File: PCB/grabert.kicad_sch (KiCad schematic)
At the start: 72 parts, among them J1 Conn_01x02, J2 Conn_01x02, J3 Conn_01x05, J4 USB_C_Receptacle_USB2.0, J5 SSD1306, SW0_0 1.00u, SW0_1 1.00u, SW0_10 1.00u, SW0_11 1.00u, SW0_12 1.00u, SW0_13-14 2.00u_or_1.00and1.00, SW0_2 1.00u, SW0_3 1.00u, SW0_4 1.00u, SW0_5 1.00u, SW0_6 1.00u, SW0_7 1.00u, SW0_8 1.00u, SW0_9 1.00u, SW1 RotaryEncoder_Switch, SW1_0 1.50u, SW1_1 1.00u, SW1_10 1.00u, SW1_11 1.00u, SW1_12 1.00u, SW1_13 1.50u, SW1_2 1.00u, SW1_3 1.00u, SW1_4 1.00u, SW1_5 1.00u, SW1_6 1.00u, SW1_7 1.00u, SW1_8 1.00u, SW1_9 1.00u, SW2_0 1.75u_stepped_caps_lock, SW2_1 1.00u, SW2_10 1.00u, SW2_11 1.00u, SW2_12 2.25u, SW2_2 1.00u, SW2_3 1.00u, SW2_4 1.00u, SW2_5 1.00u, SW2_6 1.00u, SW2_7 1.00u, SW2_8 1.00u, SW2_9 1.00u, SW3_0-1 2.25u_or_1.25and1.00, SW3_10 1.00u, SW3_11 1.00u, SW3_12-13 2.75u_or_1.75and1.00, SW3_2 1.00u, SW3_3 1.00u, SW3_4 1.00u, SW3_5 1.00u, SW3_6 1.00u, SW3_7 1.00u, SW3_8 1.00u, SW3_9 1.00u, SW4_0 1.25u, SW4_1 1.25u, SW4_2 1.25u, SW4_3 6.25u, SW4_4-8 4x1.25u_or_5x1.00u, U1 AMS1117-3.3, U2 STM32F072V8Tx

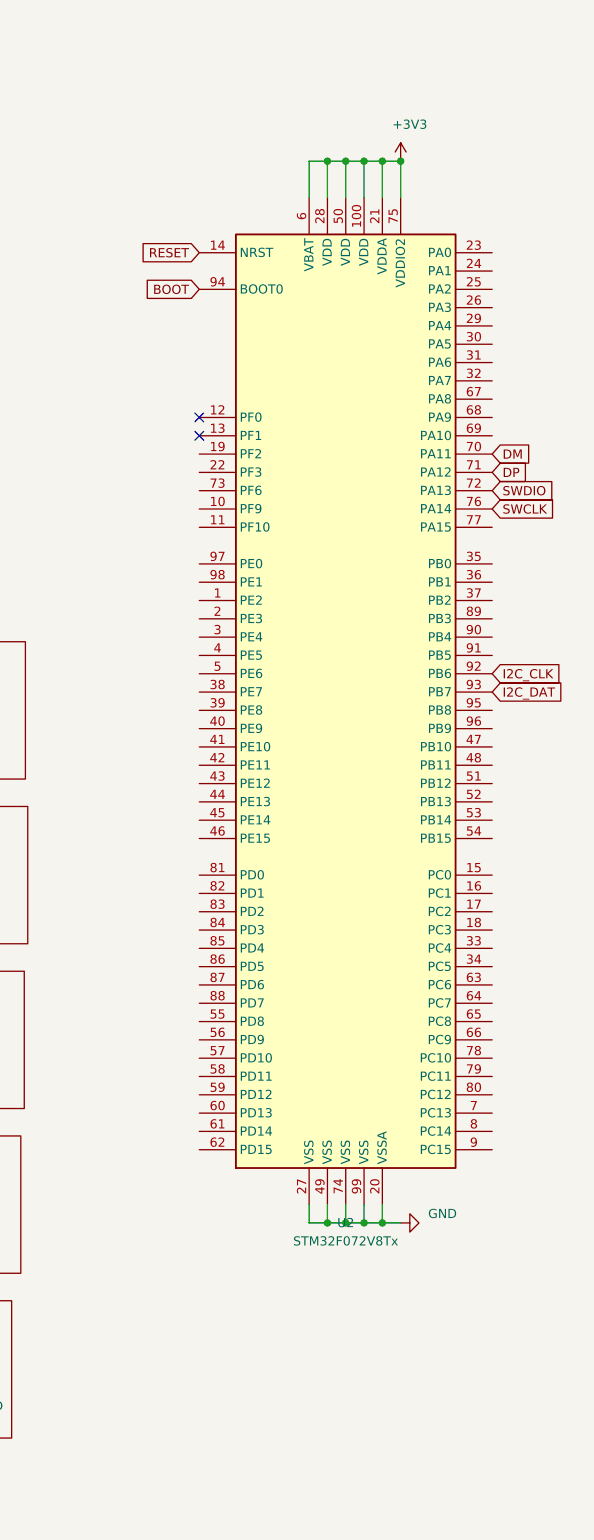
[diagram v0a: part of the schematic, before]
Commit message: Switch inputs linked to mcu
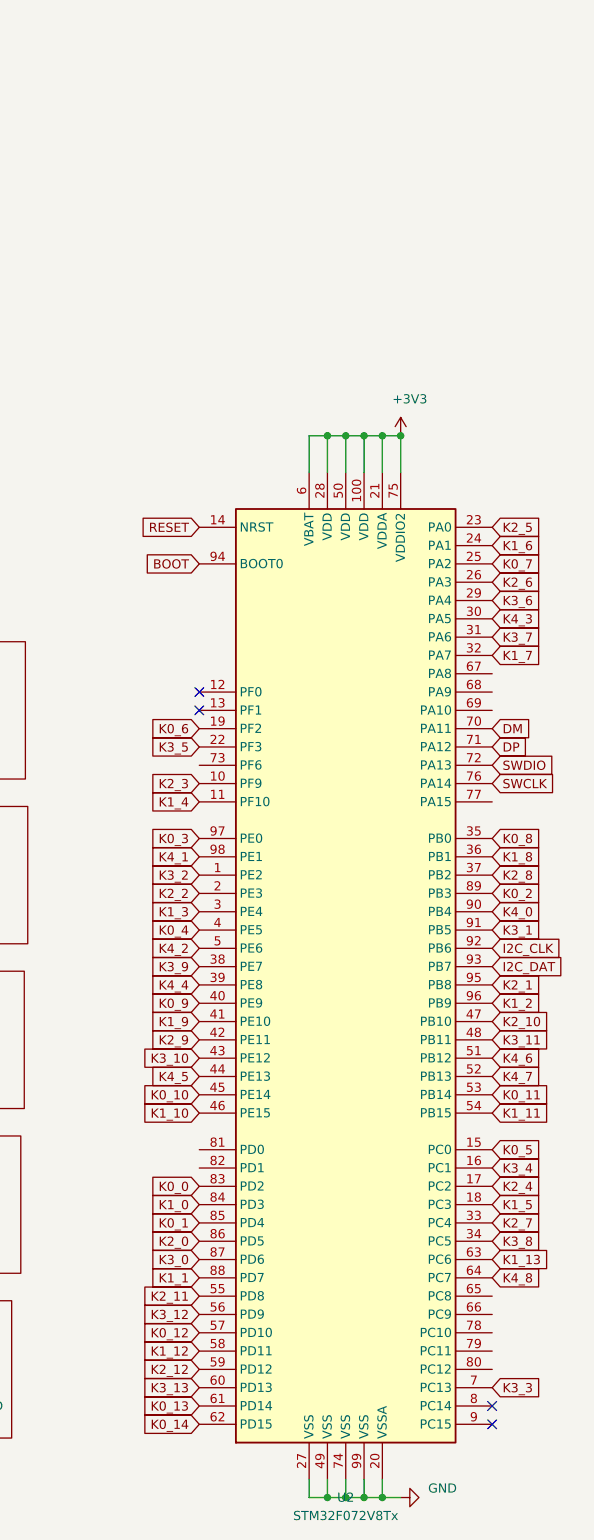
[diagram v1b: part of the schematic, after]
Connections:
- net K0_0: now also U2.83 (PD2)
- net K0_1: now also U2.85 (PD4)
- net K0_10: now also U2.45 (PE14)
- net K0_11: now also U2.53 (PB14)
- net K0_12: now also U2.57 (PD10)
- net K0_13: now also U2.61 (PD14)
- net K0_14: now also U2.62 (PD15)
- net K0_2: now also U2.89 (PB3)
- net K0_3: now also U2.97 (PE0)
- net K0_4: now also U2.4 (PE5)
- net K0_5: now also U2.15 (PC0)
- net K0_6: now also U2.19 (PF2)
- net K0_7: now also U2.25 (PA2)
- net K0_8: now also U2.35 (PB0)
- net K0_9: now also U2.40 (PE9)
- net K1_0: now also U2.84 (PD3)
- net K1_1: now also U2.88 (PD7)
- net K1_10: now also U2.46 (PE15)
- net K1_11: now also U2.54 (PB15)
- net K1_12: now also U2.58 (PD11)
- net K1_13: now also U2.63 (PC6)
- net K1_2: now also U2.96 (PB9)
- net K1_3: now also U2.3 (PE4)
- net K1_4: now also U2.11 (PF10)
- net K1_5: now also U2.18 (PC3)
- net K1_6: now also U2.24 (PA1)
- net K1_7: now also U2.32 (PA7)
- net K1_8: now also U2.36 (PB1)
- net K1_9: now also U2.41 (PE10)
- net K2_0: now also U2.86 (PD5)
- net K2_1: now also U2.95 (PB8)
- net K2_10: now also U2.47 (PB10)
- net K2_11: now also U2.55 (PD8)
- net K2_12: now also U2.59 (PD12)
- net K2_2: now also U2.2 (PE3)
- net K2_3: now also U2.10 (PF9)
- net K2_4: now also U2.17 (PC2)
- net K2_5: now also U2.23 (PA0)
- net K2_6: now also U2.26 (PA3)
- net K2_7: now also U2.33 (PC4)
- net K2_8: now also U2.37 (PB2)
- net K2_9: now also U2.42 (PE11)
- net K3_0: now also U2.87 (PD6)
- net K3_1: now also U2.91 (PB5)
- net K3_10: now also U2.43 (PE12)
- net K3_11: now also U2.48 (PB11)
- net K3_12: now also U2.56 (PD9)
- net K3_13: now also U2.60 (PD13)
- net K3_2: now also U2.1 (PE2)
- net K3_3: now also U2.7 (PC13)
- net K3_4: now also U2.16 (PC1)
- net K3_5: now also U2.22 (PF3)
- net K3_6: now also U2.29 (PA4)
- net K3_7: now also U2.31 (PA6)
- net K3_8: now also U2.34 (PC5)
- net K3_9: now also U2.38 (PE7)
- net K4_0: now also U2.90 (PB4)
- net K4_1: now also U2.98 (PE1)
- net K4_2: now also U2.5 (PE6)
- net K4_3: now also U2.30 (PA5)
- net K4_4: now also U2.39 (PE8)
- net K4_5: now also U2.44 (PE13)
- net K4_6: now also U2.51 (PB12)
- net K4_7: now also U2.52 (PB13)
- net K4_8: now also U2.64 (PC7)
- no-connect marks 6 -> 8
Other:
- moved on the sheet: U2

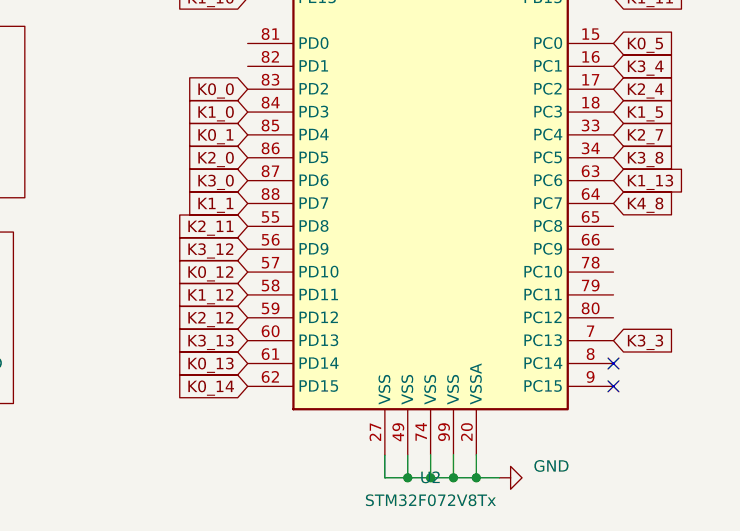
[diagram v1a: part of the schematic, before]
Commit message: right switch traces
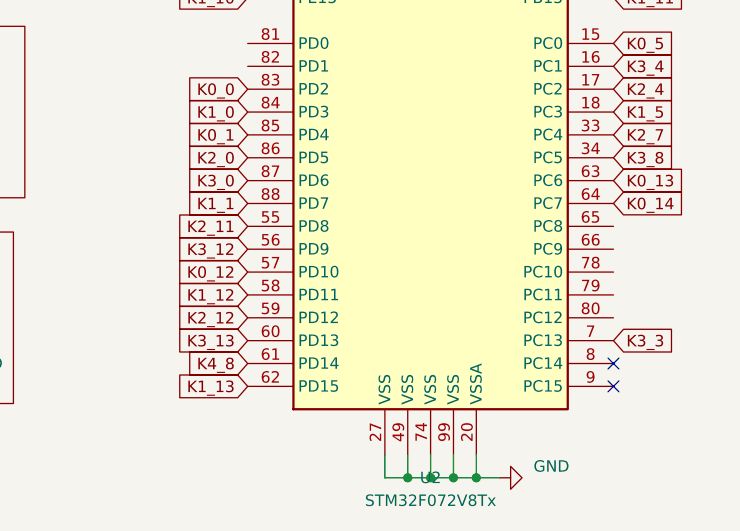
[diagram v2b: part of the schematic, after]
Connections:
- net K0_13: now also U2.63 (PC6); no longer U2.61 (PD14)
- net K0_14: now also U2.64 (PC7); no longer U2.62 (PD15)
- net K1_13: now also U2.62 (PD15); no longer U2.63 (PC6)
- net K4_8: now also U2.61 (PD14); no longer U2.64 (PC7)
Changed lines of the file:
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@@
   (junction (at 378.46 226.06) (diameter 1.016) (color 0 0 0 0))
   (junction (at 381 78.74) (diameter 1.016) (color 0 0 0 0))
+  (no_connect (at 314.96 40.64))
+  (no_connect (at 393.7 213.36))
+  (no_connect (at 353.06 116.84))
+  (no_connect (at 314.96 36.83))
   (no_connect (at 228.6 62.23))
+  (no_connect (at 393.7 215.9))
+  (no_connect (at 228.6 64.77))
   (no_connect (at 353.06 114.3))
-  (no_connect (at 314.96 40.64))
-  (no_connect (at 314.96 36.83))
-  (no_connect (at 228.6 64.77))
-  (no_connect (at 353.06 116.84))
-  (no_connect (at 393.7 213.36))
-  (no_connect (at 393.7 215.9))
   (wire (pts (xy 38.1 38.1) (xy 45.72 38.1))
     (stroke (width 0) (type solid) (color 0 0 0 0))
@@
     (effects (font (size 1.27 1.27)) (justify right))
   )
-  (global_label "K0_13" (shape input) (at 353.06 213.36 180)
-    (effects (font (size 1.27 1.27)) (justify right))
-  )
-  (global_label "K0_14" (shape input) (at 353.06 215.9 180)
+  (global_label "K4_8" (shape input) (at 353.06 213.36 180)
+    (effects (font (size 1.27 1.27)) (justify right))
+  )
+  (global_label "K1_13" (shape input) (at 353.06 215.9 180)
     (effects (font (size 1.27 1.27)) (justify right))
   )
@@
     (effects (font (size 1.27 1.27)) (justify left))
   )
-  (global_label "K1_13" (shape input) (at 393.7 193.04 0)
-    (effects (font (size 1.27 1.27)) (justify left))
-  )
-  (global_label "K4_8" (shape input) (at 393.7 195.58 0)
-    (effects (font (size 1.27 1.27)) (justify left))
-  )
+  (global_label "K0_13" (shape input) (at 393.7 193.04 0)
+    (effects (font (size 1.27 1.27)) (justify left))
+  )
+  (global_label "K0_14" (shape input) (at 393.7 195.58 0)
+    (effects (font (size 1.27 1.27)) (justify left))
+  )

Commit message: Routed PCB
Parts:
- added J6: Conn_01x03, Connector_PinHeader_2.54mm:PinHeader_1x03_P2.54mm_Vertical, symbol Connector_Generic:Conn_01x03
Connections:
- net +5V: now also J6.3 (Pin_3)
- net ENC_A: now also U2.66 (PC9)
- net ENC_B: now also U2.67 (PA8)
- net ENC_SW: now also U2.65 (PC8)
- net GND: now also J6.2 (Pin_2)
- net PA9: now reaches U2.68 (PA9)
- net PA9: now also J6.1 (Pin_1)
- net DM renamed D_N
- net DP renamed D_P
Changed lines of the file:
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@@
   (junction (at 378.46 226.06) (diameter 1.016) (color 0 0 0 0))
   (junction (at 381 78.74) (diameter 1.016) (color 0 0 0 0))
-  (no_connect (at 314.96 40.64))
-  (no_connect (at 393.7 213.36))
+  (no_connect (at 393.7 215.9))
+  (no_connect (at 353.06 114.3))
+  (no_connect (at 228.6 64.77))
+  (no_connect (at 228.6 62.23))
   (no_connect (at 353.06 116.84))
   (no_connect (at 314.96 36.83))
-  (no_connect (at 228.6 62.23))
-  (no_connect (at 393.7 215.9))
-  (no_connect (at 228.6 64.77))
-  (no_connect (at 353.06 114.3))
+  (no_connect (at 393.7 213.36))
+  (no_connect (at 314.96 40.64))
   (wire (pts (xy 38.1 38.1) (xy 45.72 38.1))
     (stroke (width 0) (type solid) (color 0 0 0 0))
@@
     (effects (font (size 1.27 1.27)) (justify right))
   )
+  (global_label "PA9" (shape input) (at 95.25 69.85 180)
+    (effects (font (size 1.27 1.27)) (justify right))
+  )
   (global_label "K3_3" (shape input) (at 96.52 185.42 90)
     (effects (font (size 1.27 1.27)) (justify left))
@@
     (effects (font (size 1.27 1.27)) (justify left))
   )
-  (global_label "DM" (shape input) (at 231.14 46.99 0)
-    (effects (font (size 1.27 1.27)) (justify left))
-  )
-  (global_label "DP" (shape input) (at 231.14 54.61 0)
+  (global_label "D_N" (shape input) (at 231.14 46.99 0)
+    (effects (font (size 1.27 1.27)) (justify left))
+  )
+  (global_label "D_P" (shape input) (at 231.14 54.61 0)
     (effects (font (size 1.27 1.27)) (justify left))
   )
@@
     (effects (font (size 1.27 1.27)) (justify left))
   )
-  (global_label "DM" (shape input) (at 393.7 119.38 0)
-    (effects (font (size 1.27 1.27)) (justify left))
-  )
-  (global_label "DP" (shape input) (at 393.7 121.92 0)
+  (global_label "ENC_B" (shape input) (at 393.7 111.76 0)
+    (effects (font (size 1.27 1.27)) (justify left))
+  )
+  (global_label "PA9" (shape input) (at 393.7 114.3 0)
+    (effects (font (size 1.27 1.27)) (justify left))
+  )
+  (global_label "D_N" (shape input) (at 393.7 119.38 0)
+    (effects (font (size 1.27 1.27)) (justify left))
+  )
+  (global_label "D_P" (shape input) (at 393.7 121.92 0)
     (effects (font (size 1.27 1.27)) (justify left))
   )
@@
   )
   (global_label "K0_14" (shape input) (at 393.7 195.58 0)
+    (effects (font (size 1.27 1.27)) (justify left))
+  )
+  (global_label "ENC_SW" (shape input) (at 393.7 198.12 0)
+    (effects (font (size 1.27 1.27)) (justify left))
+  )
+  (global_label "ENC_A" (shape input) (at 393.7 200.66 0)
     (effects (font (size 1.27 1.27)) (justify left))
   )
@@
     )
   )
+  (symbol (lib_id "power:+5V") (at 95.25 74.93 180) (unit 1)
+    (in_bom yes) (on_board yes)
+    (property "Reference" "#PWR0187" (id 0) (at 95.25 71.12 0)
+      (effects (font (size 1.27 1.27)) hide)
+    )
+    (property "Value" "+5V" (id 1) (at 93.98 80.01 0))
+    (property "Footprint" "" (id 2) (at 95.25 74.93 0)
+      (effects (font (size 1.27 1.27)) hide)
+    )
+    (property "Datasheet" "" (id 3) (at 95.25 74.93 0)
+      (effects (font (size 1.27 1.27)) hide)
+    )
+  )
   (symbol (lib_id "power:+5V") (at 133.35 45.72 0) (unit 1)
     (in_bom yes) (on_board yes)
@@
     )
     (property "Datasheet" "" (id 3) (at 95.25 52.07 0)
+      (effects (font (size 1.27 1.27)) hide)
+    )
+  )
+  (symbol (lib_id "power:GND") (at 95.25 72.39 270) (unit 1)
+    (in_bom yes) (on_board yes)
+    (property "Reference" "#PWR0186" (id 0) (at 88.9 72.39 0)
+      (effects (font (size 1.27 1.27)) hide)
+    )
+    (property "Value" "GND" (id 1) (at 90.17 73.66 0))
+    (property "Footprint" "" (id 2) (at 95.25 72.39 0)
+      (effects (font (size 1.27 1.27)) hide)
+    )
+    (property "Datasheet" "" (id 3) (at 95.25 72.39 0)
       (effects (font (size 1.27 1.27)) hide)
     )
@@
     )
     (property "Datasheet" "~" (id 3) (at 163.83 49.53 0)
+      (effects (font (size 1.27 1.27)) hide)
+    )
+  )
+  (symbol (lib_id "Connector_Generic:Conn_01x03") (at 100.33 72.39 0) (unit 1)
+    (in_bom yes) (on_board yes)
+    (property "Reference" "J6" (id 0) (at 102.87 71.12 0)
+      (effects (font (size 1.27 1.27)) (justify left))
+    )
+    (property "Value" "Conn_01x03" (id 1) (at 102.87 73.66 0)
+      (effects (font (size 1.27 1.27)) (justify left))
+    )
+    (property "Footprint" "Connector_PinHeader_2.54mm:PinHeader_1x03_P2.54mm_Vertical" (id 2) (at 100.33 72.39 0)
+      (effects (font (size 1.27 1.27)) hide)
+    )
+    (property "Datasheet" "~" (id 3) (at 100.33 72.39 0)
       (effects (font (size 1.27 1.27)) hide)
     )
@@
       (reference "#PWR0185") (unit 1) (value "GND") (footprint "")
     )
+    (path "/a1c60f5c-d5c9-4cf4-9c73-d610f02073db"
+      (reference "#PWR0186") (unit 1) (value "GND") (footprint "")
+    )
+    (path "/08f5b989-ff5a-41d6-bebc-56b8992d3159"
+      (reference "#PWR0187") (unit 1) (value "+5V") (footprint "")
+    )
     (path "/54f5ef39-f28e-4031-8773-1daf6a8c137a"
       (reference "C1") (unit 1) (value "10uF") (footprint "Capacitor_SMD:C_0603_1608Metric")
@@
       (reference "J5") (unit 1) (value "SSD1306") (footprint "kobuss-footprint:SSD1306")
     )
+    (path "/88c3d9e3-283d-4ee8-b49f-3da037b4c0a8"
+      (reference "J6") (unit 1) (value "Conn_01x03") (footprint "Connector_PinHeader_2.54mm:PinHeader_1x03_P2.54mm_Vertical")
+    )
     (path "/f87f60e9-3ad6-416d-9c22-25804653c0b5"

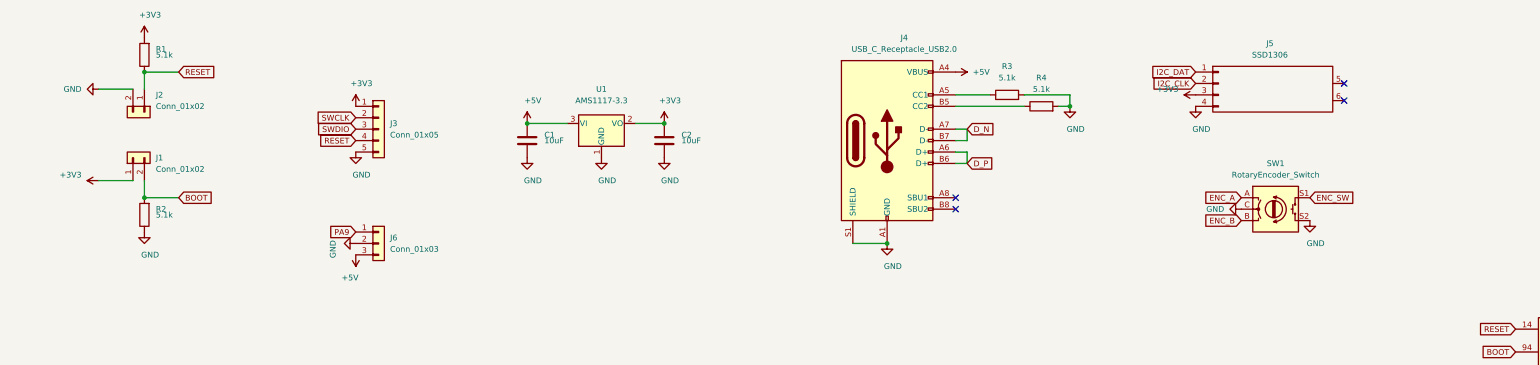
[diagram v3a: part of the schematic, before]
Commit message: pcb: added 100nF bypass caps
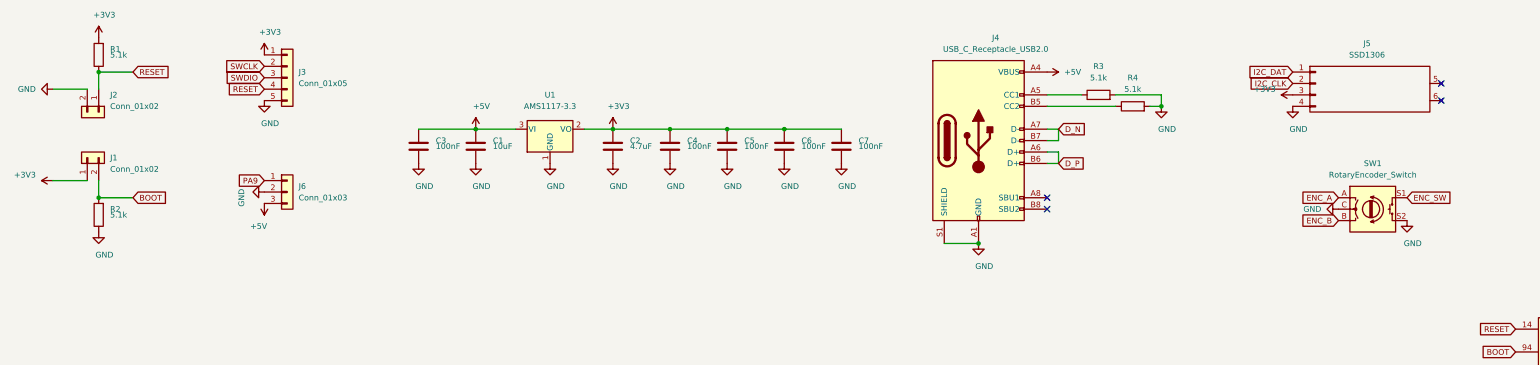
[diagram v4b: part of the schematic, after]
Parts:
- added C3, C4, C5, C6, C7: 100nF, Capacitor_SMD:C_0603_1608Metric, symbol Device:C
- C2: value 10uF -> 4.7uF
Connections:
- net +3V3: now also C4.1, C5.1, C6.1, C7.1
- net +5V: now also C3.1
- net GND: now also C3.2, C4.2, C5.2, C6.2, C7.2
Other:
- moved on the sheet: C1, C2, J1, J2, J3, J4, J6, R1, R2, R3, R4, SW1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
